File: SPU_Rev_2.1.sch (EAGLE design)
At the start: 251 parts, among them Q1 12MHz

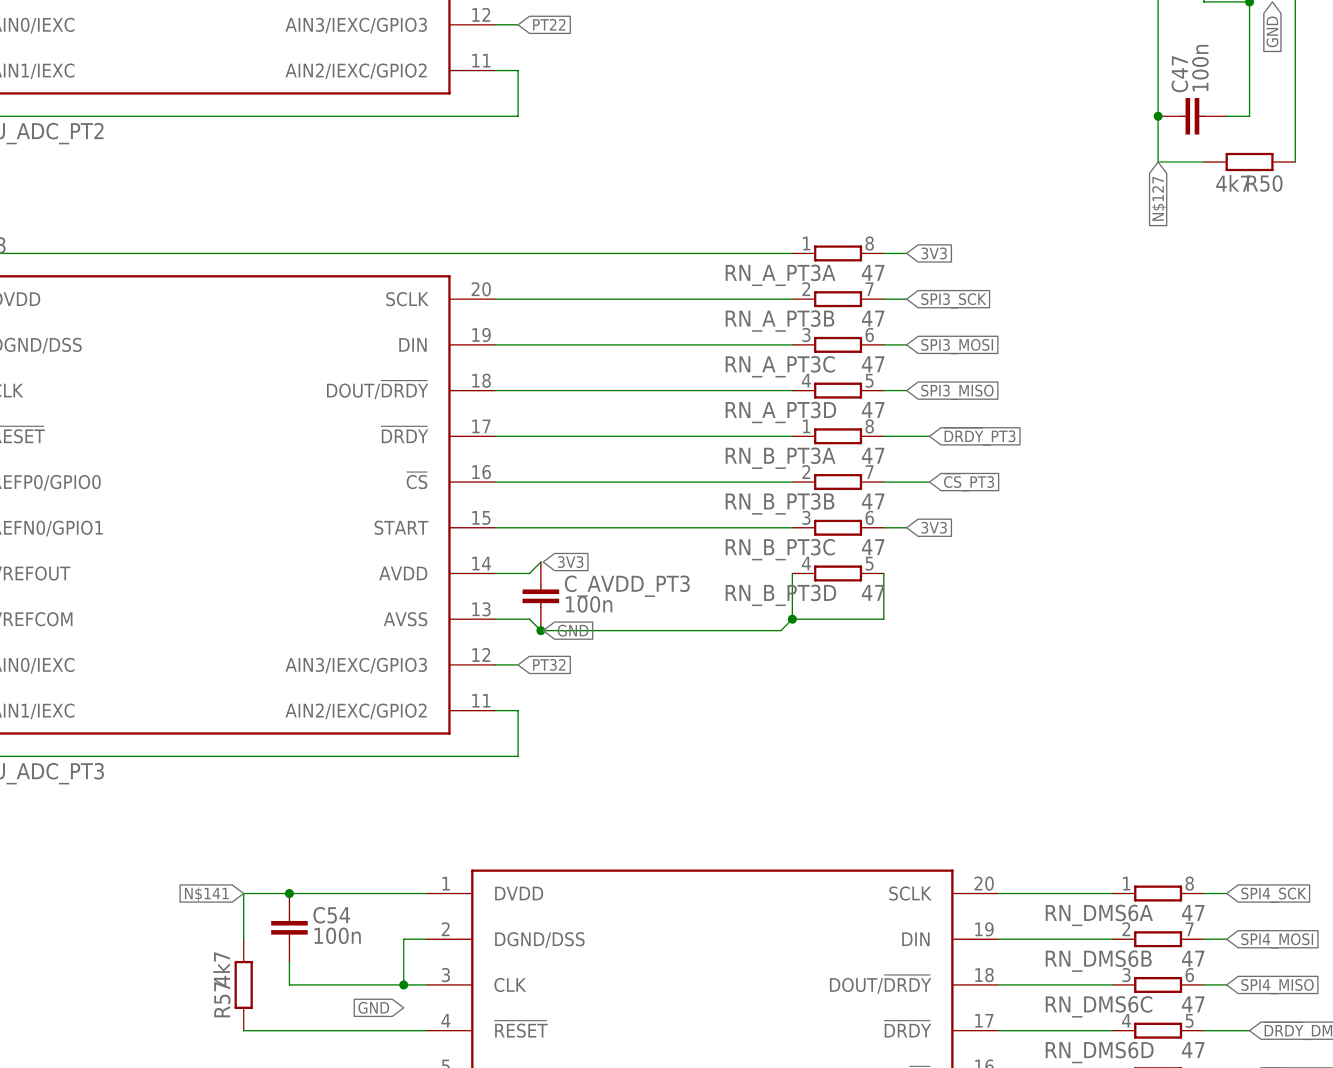
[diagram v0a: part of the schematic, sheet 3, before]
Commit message: airwire fixed (2x)
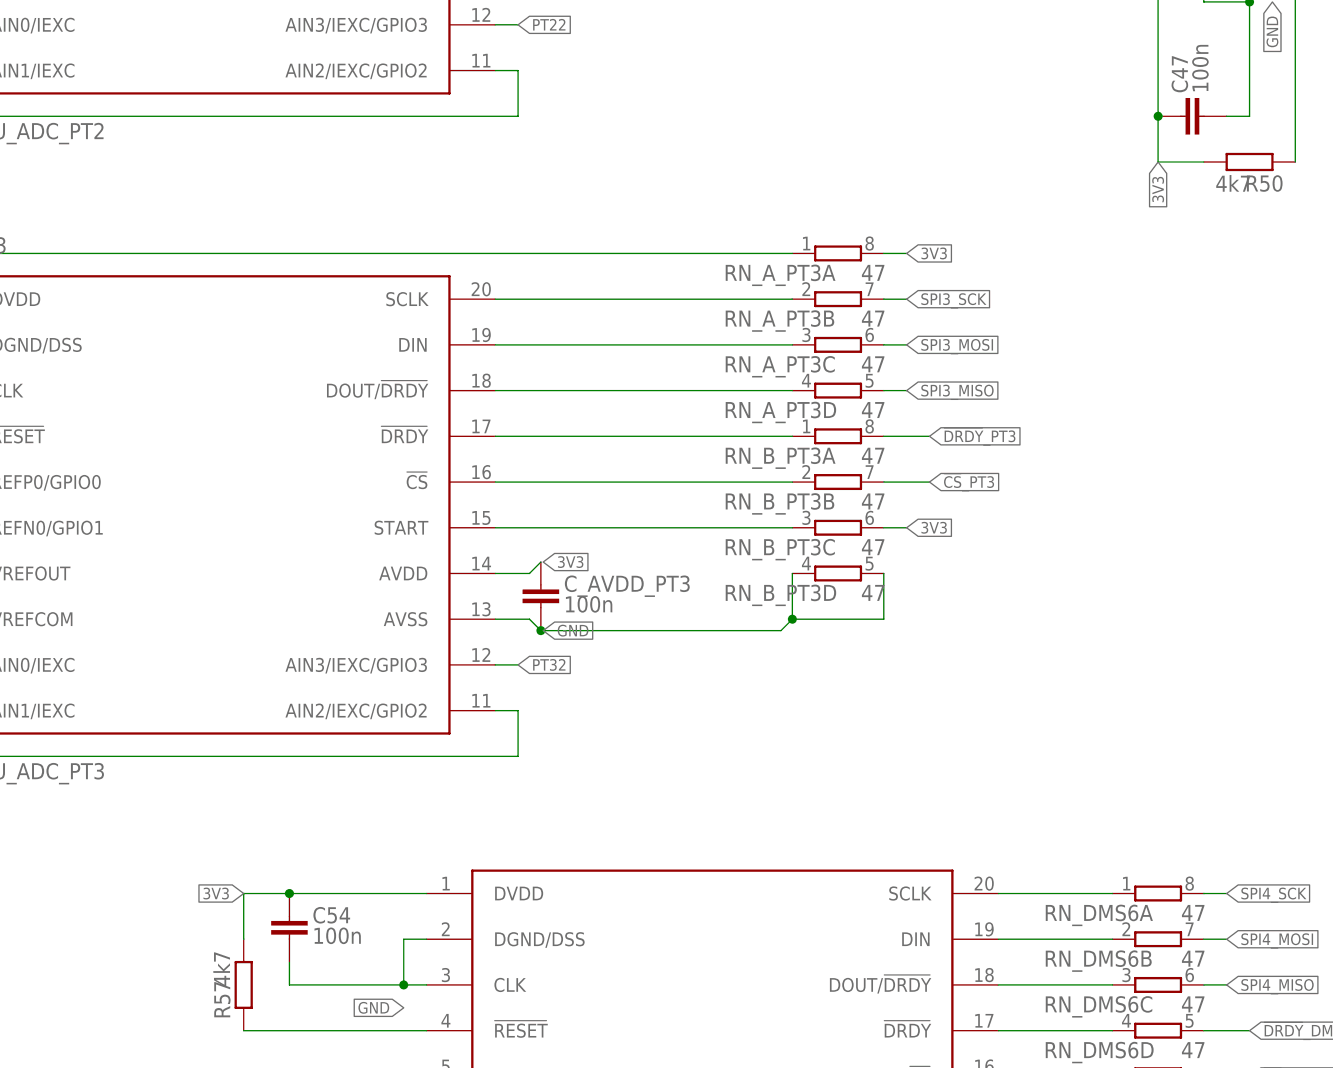
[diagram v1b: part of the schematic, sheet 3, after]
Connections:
- removed net N$127: C47.1, R50.1, U_ADC_DMS5.DVDD
- removed net N$141: C54.1, R57.1, U_ADC_DMS6.DVDD
- net 3V3: now also C47.1, C54.1, R50.1, R57.1, U_ADC_DMS5.DVDD, U_ADC_DMS6.DVDD
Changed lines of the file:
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@@
 <label x="157.48" y="96.52" size="1.27" layer="95" rot="R180" xref="yes"/>
+</segment>
+<segment>
+<wire x1="134.62" y1="-314.96" x2="119.38" y2="-314.96" width="0.1524" layer="91"/>
+<label x="114.3" y="-314.96" size="1.27" layer="95" rot="R180" xref="yes"/>
+<wire x1="119.38" y1="-314.96" x2="114.3" y2="-314.96" width="0.1524" layer="91"/>
+<junction x="119.38" y="-314.96"/>
+<wire x1="114.3" y1="-314.96" x2="114.3" y2="-320.04" width="0.1524" layer="91"/>
+<pinref part="U_ADC_DMS6" gate="G$1" pin="DVDD"/>
+<pinref part="C54" gate="G$1" pin="1"/>
+<pinref part="R57" gate="G$1" pin="1"/>
+</segment>
+<segment>
+<wire x1="215.9" y1="-213.36" x2="215.9" y2="-228.6" width="0.1524" layer="91"/>
+<label x="215.9" y="-233.68" size="1.27" layer="95" rot="R270" xref="yes"/>
+<wire x1="215.9" y1="-228.6" x2="215.9" y2="-233.68" width="0.1524" layer="91"/>
+<junction x="215.9" y="-228.6"/>
+<wire x1="215.9" y1="-233.68" x2="220.98" y2="-233.68" width="0.1524" layer="91"/>
+<pinref part="U_ADC_DMS5" gate="G$1" pin="DVDD"/>
+<pinref part="C47" gate="G$1" pin="1"/>
+<pinref part="R50" gate="G$1" pin="1"/>
 </segment>
 </net>
@@
 </segment>
 </net>
-<net name="N$127" class="0">
-<segment>
-<wire x1="215.9" y1="-213.36" x2="215.9" y2="-228.6" width="0.1524" layer="91"/>
-<label x="215.9" y="-233.68" size="1.27" layer="95" rot="R270" xref="yes"/>
-<wire x1="215.9" y1="-228.6" x2="215.9" y2="-233.68" width="0.1524" layer="91"/>
-<junction x="215.9" y="-228.6"/>
-<wire x1="215.9" y1="-233.68" x2="220.98" y2="-233.68" width="0.1524" layer="91"/>
-<pinref part="U_ADC_DMS5" gate="G$1" pin="DVDD"/>
-<pinref part="C47" gate="G$1" pin="1"/>
-<pinref part="R50" gate="G$1" pin="1"/>
-</segment>
-</net>
 <net name="N$128" class="0">
 <segment>
@@
 </segment>
 </net>
-<net name="N$141" class="0">
-<segment>
-<wire x1="134.62" y1="-314.96" x2="119.38" y2="-314.96" width="0.1524" layer="91"/>
-<label x="114.3" y="-314.96" size="1.27" layer="95" rot="R180" xref="yes"/>
-<wire x1="119.38" y1="-314.96" x2="114.3" y2="-314.96" width="0.1524" layer="91"/>
-<junction x="119.38" y="-314.96"/>
-<wire x1="114.3" y1="-314.96" x2="114.3" y2="-320.04" width="0.1524" layer="91"/>
-<pinref part="U_ADC_DMS6" gate="G$1" pin="DVDD"/>
-<pinref part="C54" gate="G$1" pin="1"/>
-<pinref part="R57" gate="G$1" pin="1"/>
-</segment>
-</net>

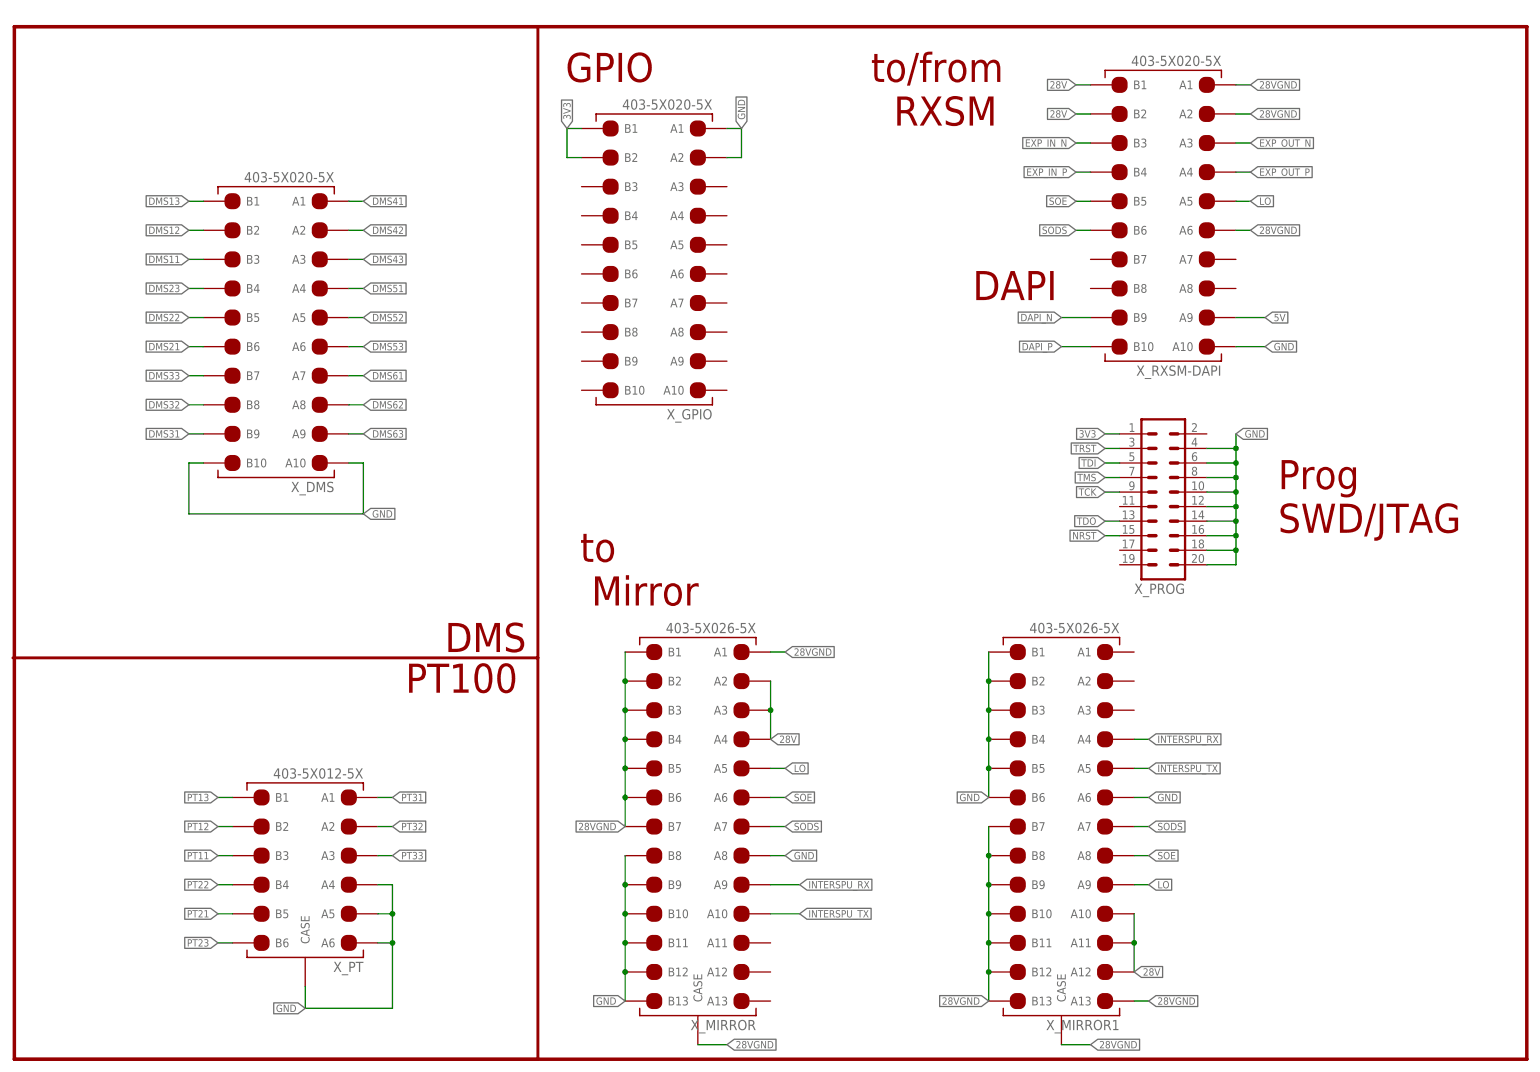
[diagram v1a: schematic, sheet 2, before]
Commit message: microsd added
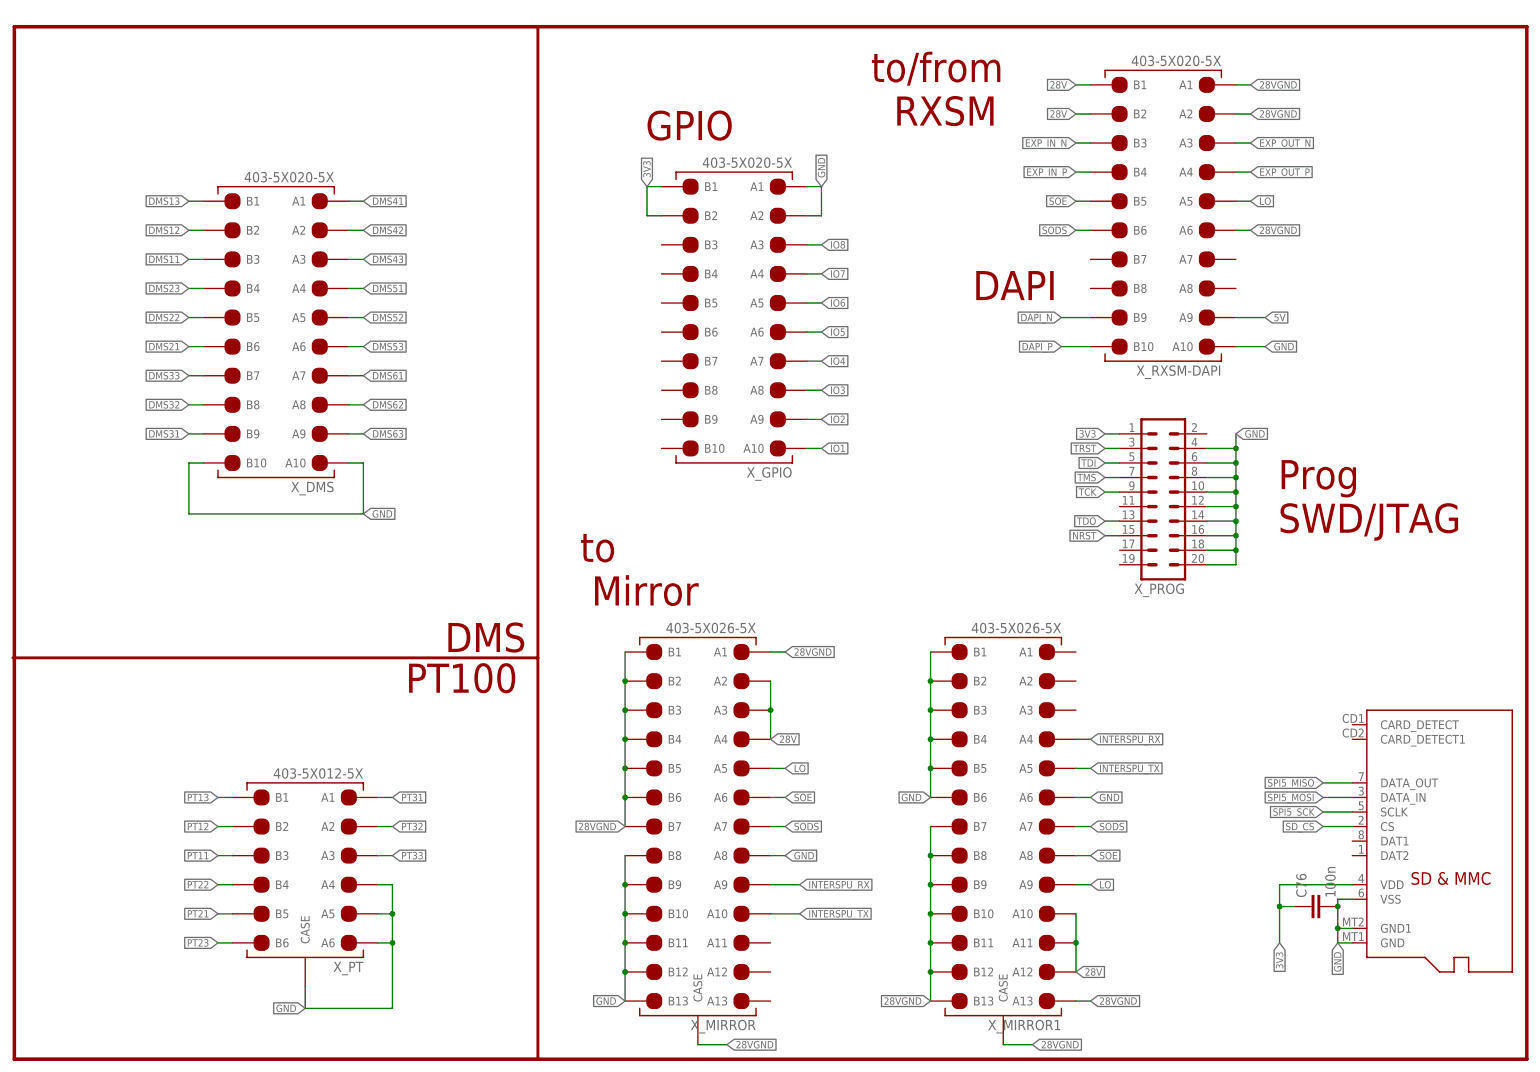
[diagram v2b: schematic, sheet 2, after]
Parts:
- added C74: 10n, rcl:C-EUC0805
- added C75: 100n, rcl:C-EUC0805
- added C76: 100n, aSparkFun:CAP0603-CAP
- added U$7: MICROSD, adafruit:MICROSD
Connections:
- new net IO1: U_STM32F779.PA3, X_GPIO.A10
- new net IO2: U_STM32F779.PH5, X_GPIO.A9
- new net IO3: U_STM32F779.PH4, X_GPIO.A8
- new net IO4: U_STM32F779.PH3, X_GPIO.A7
- new net IO5: U_STM32F779.PC3, X_GPIO.A6
- new net IO6: U_STM32F779.PC2, X_GPIO.A5
- new net IO7: U_STM32F779.PC1, X_GPIO.A4
- new net IO8: U_STM32F779.PC0, X_GPIO.A3
- new net SD_CS: U$7.CS, U_STM32F779.PF10
- new net SPI5_MISO: U$7.DATA_OUT, U_STM32F779.PF8
- new net SPI5_MOSI: U$7.DATA_IN, U_STM32F779.PF9
- new net SPI5_SCK: U$7.SCLK, U_STM32F779.PF7
- net 3V3: now also C76.1, U$7.VDD
- net 3V3REF: now also C74.2, C75.2
- net GND: now also C74.1, C75.1, C76.2, U$7.GND, U$7.GND1, U$7.VSS
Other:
- note added: "Spike/ESD protection"
- note removed: "Spike protection"
- moved on the sheet: X_GPIO, X_MIRROR1

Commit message: foo
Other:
- moved on the sheet: C1, C2, C34, C35, C36, C37, C38, C39, C40, C41, C42, C43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

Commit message: bar
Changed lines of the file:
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@@
 <text x="241.046" y="94.488" size="5.08" layer="94">Prog
 SWD/JTAG</text>
-<text x="130.556" y="163.068" size="5.08" layer="94">GPIO</text>
+<text x="135.636" y="161.798" size="5.08" layer="94">GPIO</text>
 </plain>
 <instances>

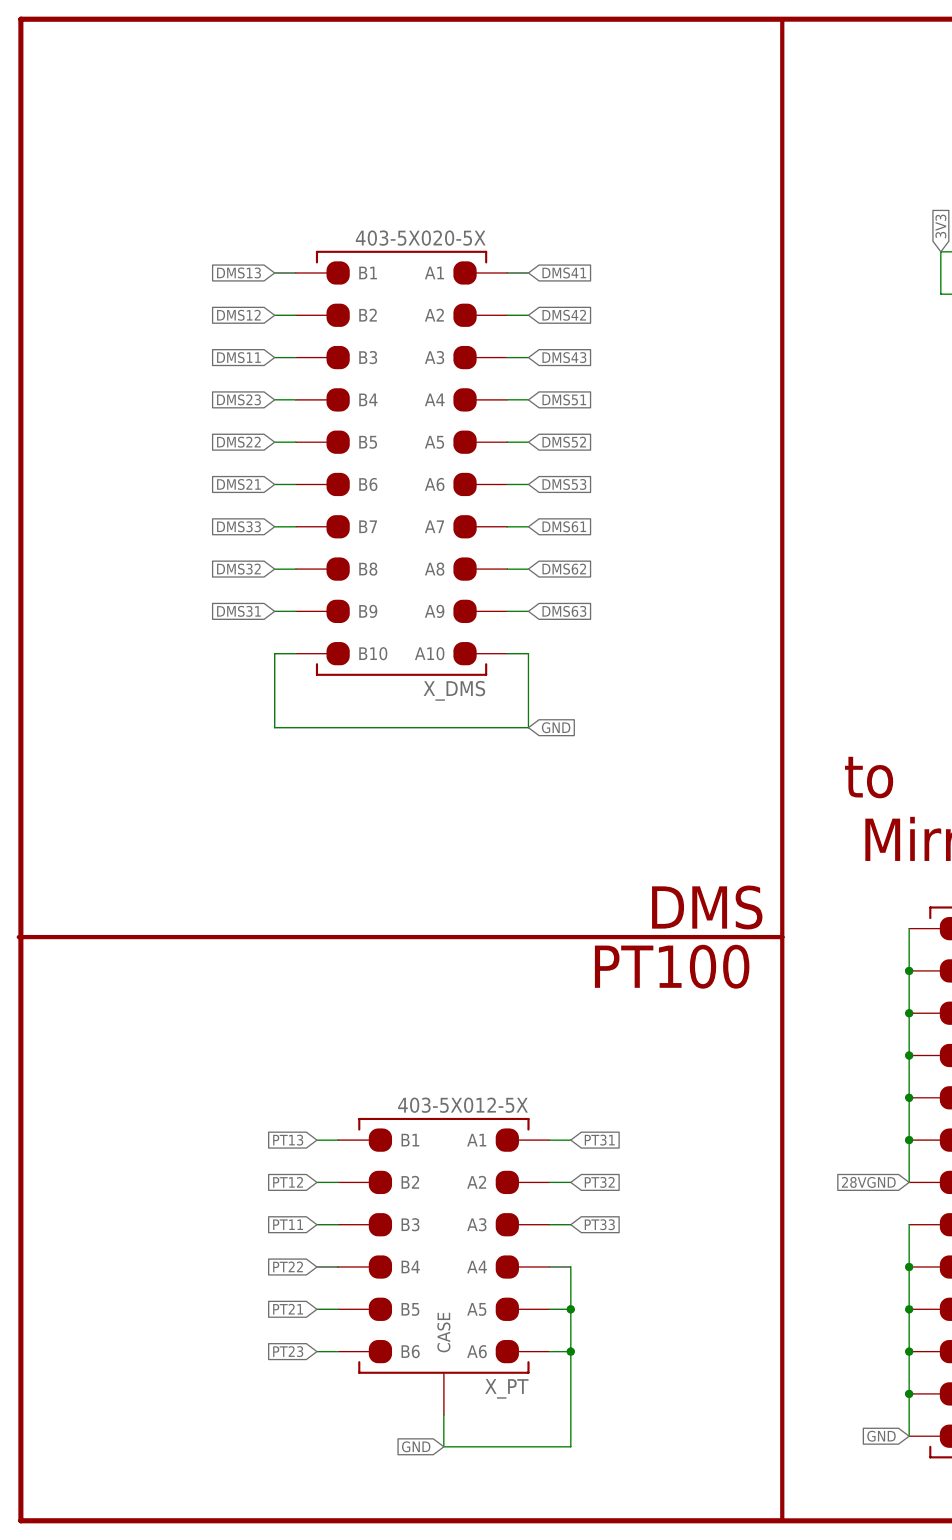
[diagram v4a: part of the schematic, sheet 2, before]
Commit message: added LWL OUT
added LWL OUT jack
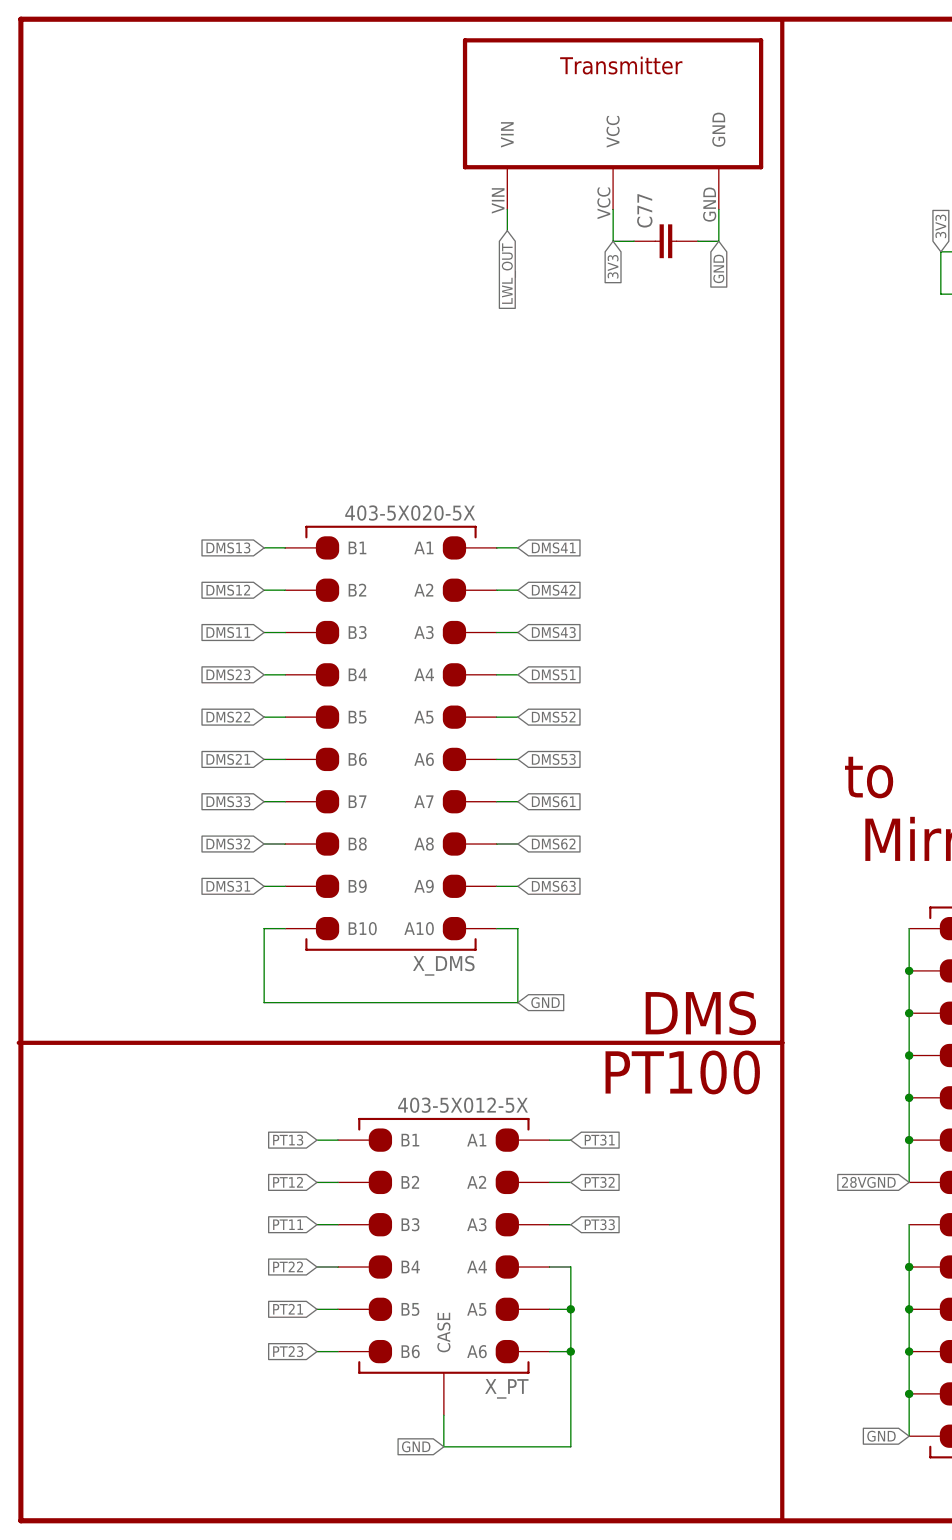
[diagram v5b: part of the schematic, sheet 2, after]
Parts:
- added C77: (no value), rcl:C-EUC1206
- added U$8: PLT131PLT131-T1, everlight-fiber-optics-spdif:PLT131PLT131-T1
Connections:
- new net LWL_OUT: U$8.VIN, U_STM32F779.PI3
- net 3V3: now also C77.1, U$8.VCC
- net GND: now also C77.2, U$8.GND
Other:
- moved on the sheet: X_DMS
